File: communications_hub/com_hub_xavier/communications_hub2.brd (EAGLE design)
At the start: 68 x 33 mm, 49 parts, among them CON1 SM04B-GHS-TB, CON2 SM04B-GHS-TB, CON3 SM02B-GHS-TB, CON6 UAVCAN_MICRO, CON7 UAVCAN_MICRO, Q1 DMN5L06K, Q2 DMN5L06K, U1 TCAN1042HVDR, U2 TCAN1042HVDR

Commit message: The board layout is completed.
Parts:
- moved Q2 96.7 mm to (62.2, 8.89)
- moved R19 95.4 mm to (58.4, 27.9), turned to 180 degrees
- moved GPIO_EXP_P17 83.1 mm to (27.9, 30.5)
- moved R13 79.5 mm to (35.6, 29.2)
- moved R21 78.3 mm to (48.3, 8.89)
- moved R22 74.8 mm to (53.3, 8.89)
- moved TP1 63.4 mm to (36.8, 2.54)
- moved TP2 62.7 mm to (33.0, 2.54)
- moved TP3 62.1 mm to (29.2, 2.54)
- moved U$4 57.9 mm to (61.0, 22.9)
- moved R7 55.8 mm to (33.0, 25.4)
- moved SJ1 54.7 mm to (66.0, 14.0), turned to 90 degrees
- moved C2 53.9 mm to (22.9, 25.4), turned to 270 degrees
- moved R5 52.6 mm to (8.89, 30.5)
- moved R14 52.4 mm to (52.1, 29.2)
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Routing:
- net GND: track 0.00 -> 300.0 mm, vias 0 -> 22
- net +3V3: track 0.00 -> 204.5 mm, vias 0 -> 10
- net +5V: track 0.00 -> 125.2 mm, vias 0 -> 3
- net I2C_GP0_SDA: track 0.00 -> 86.9 mm, vias 0 -> 2
- net I2C_GP0_SCL: track 0.00 -> 77.4 mm, vias 0 -> 2
- net CAN0_TX_T: track 0.00 -> 73.2 mm, vias 0 -> 2
- net N$9: track 0.00 -> 56.3 mm
- net N$21: track 0.00 -> 55.6 mm
- net N$14: track 0.00 -> 53.6 mm, vias 0 -> 2
- net N$23: track 0.00 -> 51.9 mm
- net N$22: track 0.00 -> 50.5 mm
- net N$13: track 0.00 -> 47.6 mm
- net CAN0_RX_T: track 0.00 -> 38.3 mm, vias 0 -> 2
- net N$24: track 0.00 -> 34.8 mm
- net N$7: track 0.00 -> 33.8 mm
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- added copper zone on layer 1, net GND

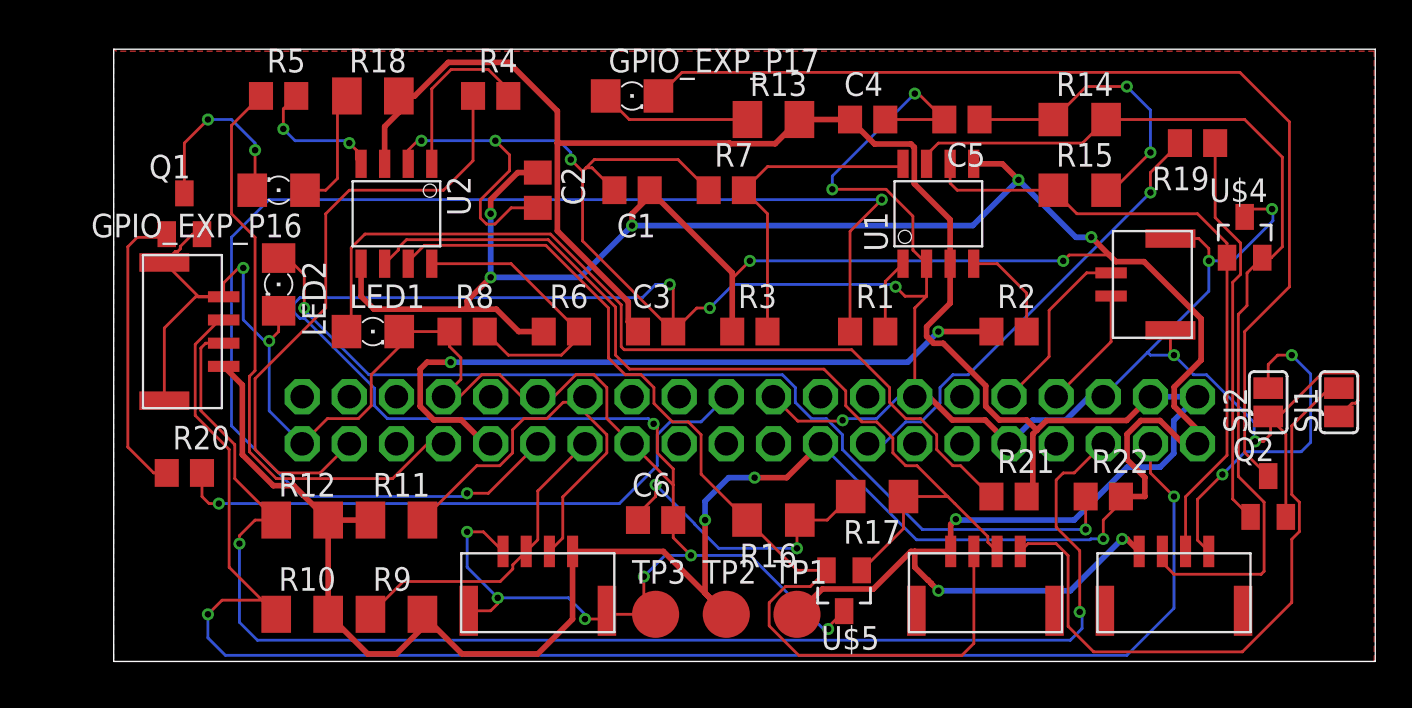
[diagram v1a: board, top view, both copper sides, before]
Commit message: Extra traces are removed, gound plane is added. Default DRC is passed. Info of the board is added as well.
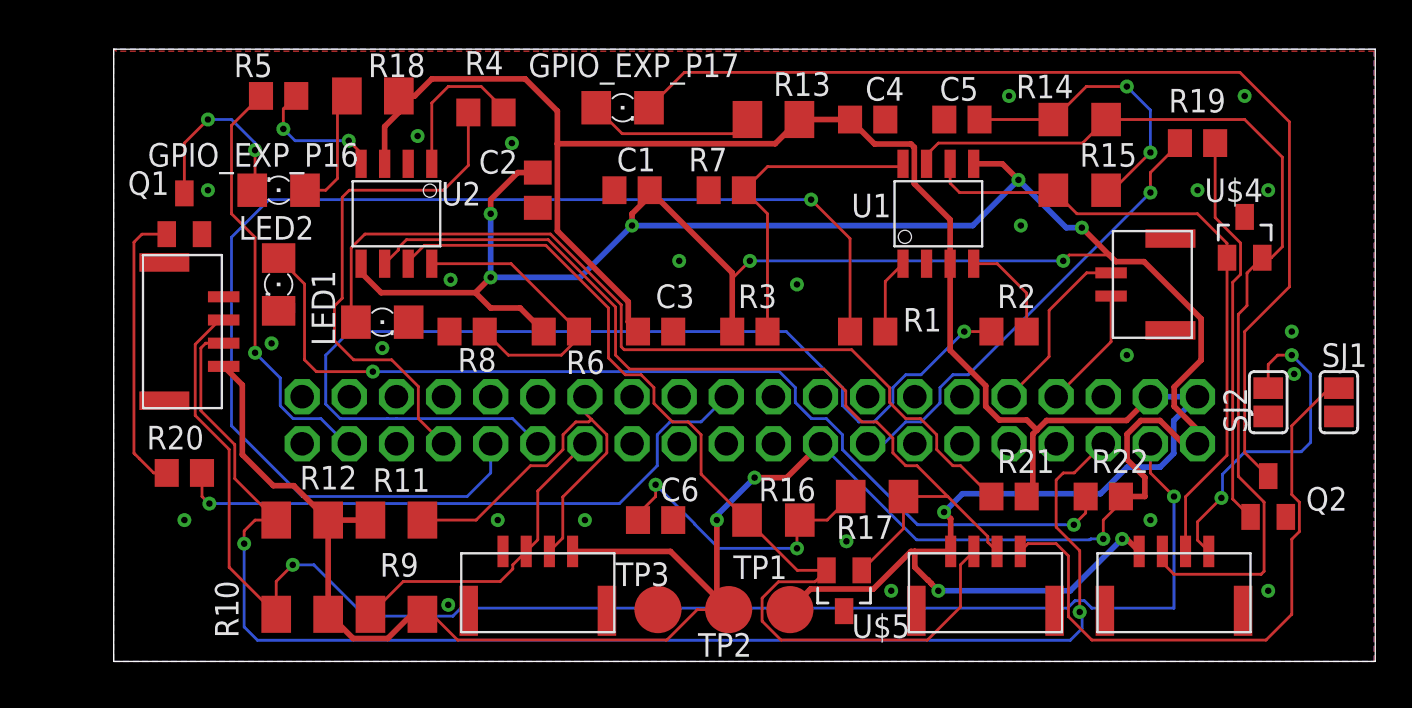
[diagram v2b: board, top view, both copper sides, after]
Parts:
- moved R4 0.92 mm to (20.1, 29.6)
- moved GPIO_EXP_P17 0.81 mm to (27.4, 29.8)
- moved LED1 0.72 mm to (14.5, 18.3)
- moved TP1 0.46 mm to (36.4, 2.79)
- moved TP3 0.28 mm to (29.3, 2.79)
- moved TP2 0.28 mm to (33.1, 2.79)
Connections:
- net CAN0_RX_T: now also JP21.29; no longer JP21.31
- net CAN0_TX_T: now also JP21.31; no longer JP21.29
- net CAN1_RX_T: now also JP21.37; no longer JP21.33
- net CAN1_TX_T: now also JP21.33; no longer JP21.37
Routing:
- net GND: track 300.0 -> 0.46 mm, vias 22 -> 24
- net CAN0_RX_T: track 38.3 -> 56.4 mm, vias 2 -> 1
- net CAN1_RX_T: track 32.3 -> 23.0 mm, vias 0 -> 1
- net I2C_GP0_SDA: track 86.9 -> 80.0 mm
- net CAN1_TX_T: track 33.1 -> 27.5 mm
- net CAN0_TX_T: track 73.2 -> 67.9 mm, vias 2 -> 1
- net N$21: track 55.6 -> 54.1 mm
- net N$28: track 9.39 -> 8.21 mm
- net +5V: track 125.2 -> 124.2 mm
- net N$3: track 8.17 -> 9.04 mm
- net N$9: track 56.3 -> 57.0 mm
- net N$13: track 47.6 -> 47.1 mm
- added copper zone on layer 16, net GND
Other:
- board text added: "Communications Hub Rev. 3.0 Karen Han 2019"

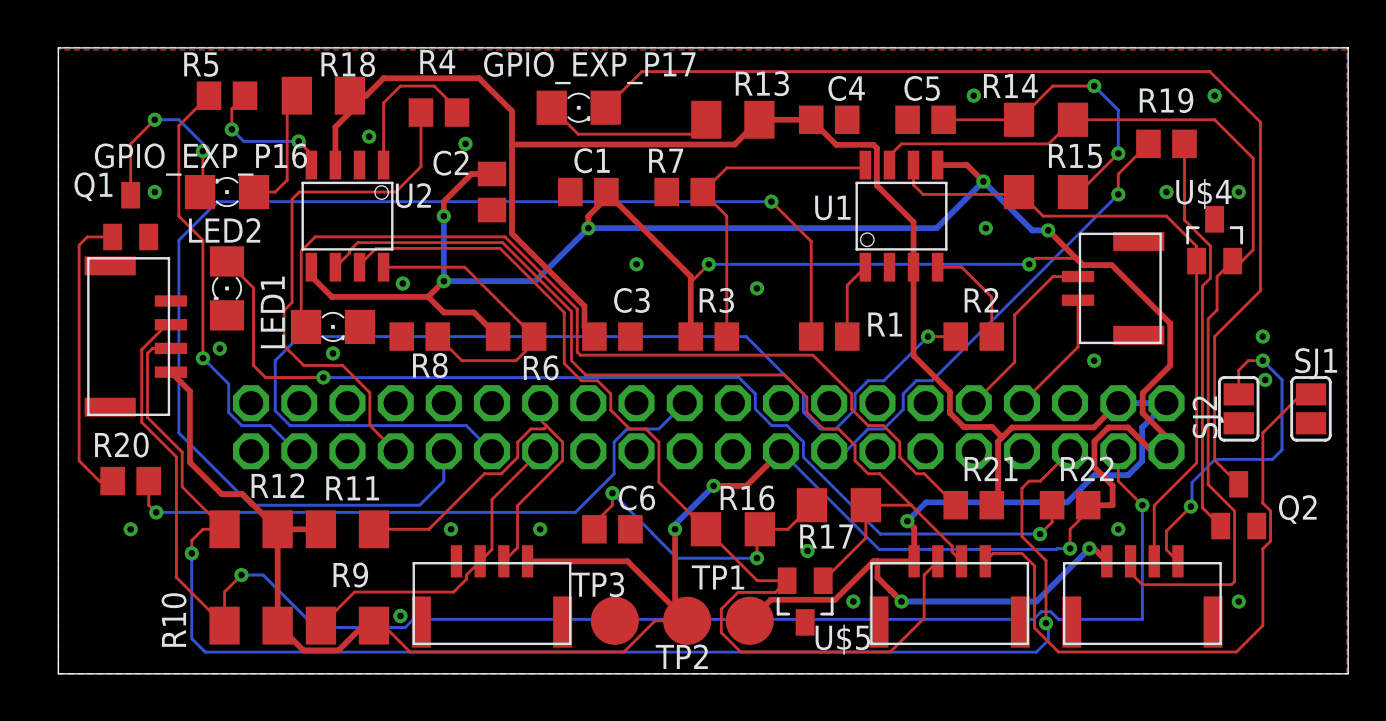
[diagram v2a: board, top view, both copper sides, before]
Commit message: Routed a couple airwires thrown in the DRC, modified some silkscreen. Project still requires BOM.
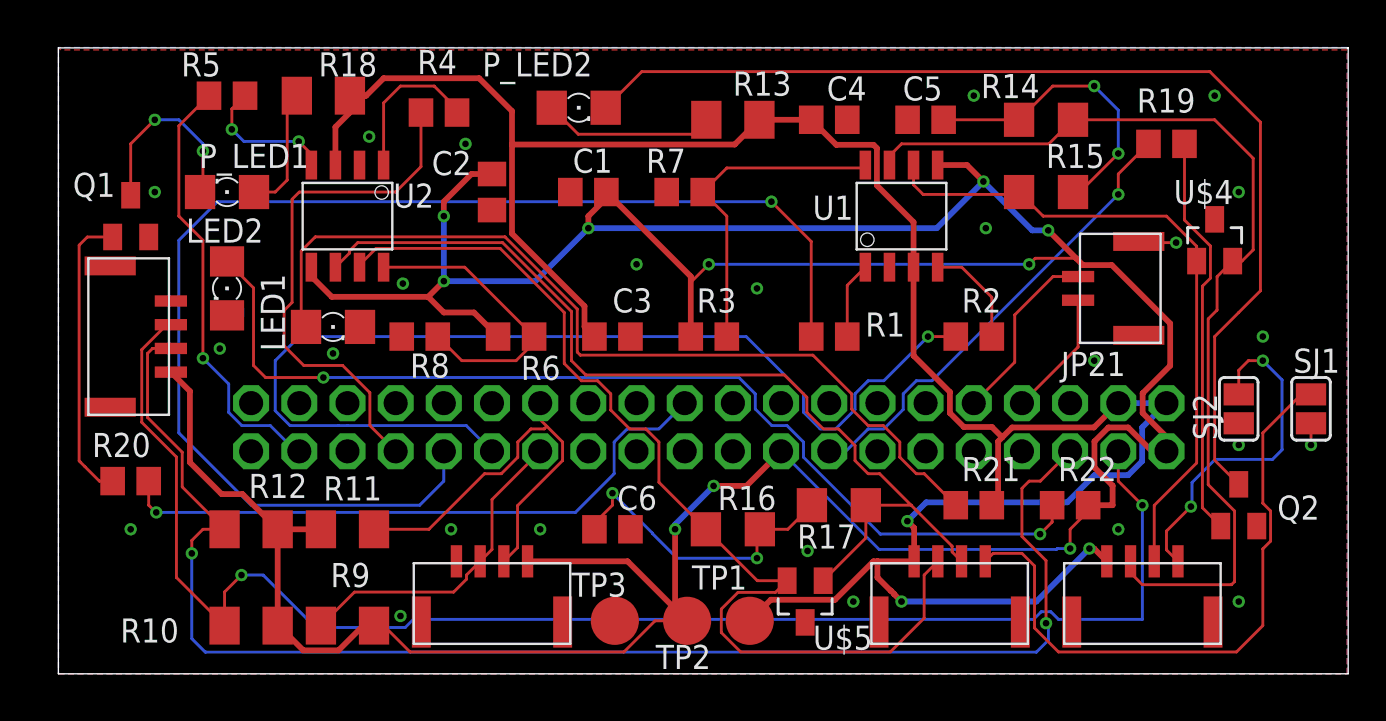
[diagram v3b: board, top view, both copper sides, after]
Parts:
- renumbered GPIO_EXP_P16 to P_LED1, GPIO_EXP_P17 to P_LED2
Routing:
- net GND: track 0.46 -> 3.60 mm, vias 24 -> 25
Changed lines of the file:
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@@
 <?xml version="1.0" encoding="utf-8"?>
 <!DOCTYPE eagle SYSTEM "eagle.dtd">
-<eagle version="9.4.0">
+<eagle version="9.2.2">
 <drawing>
 <settings>
@@
 <setting verticaltext="up"/>
 </settings>
-<grid distance="50" unitdist="mil" unit="mil" style="dots" multiple="1" display="yes" altdistance="5" altunitdist="mil" altunit="mil"/>
+<grid distance="50" unitdist="mil" unit="mil" style="dots" multiple="1" display="no" altdistance="5" altunitdist="mil" altunit="mil"/>
 <layers>
 <layer number="1" name="Top" color="4" fill="1" visible="yes" active="yes"/>
@@
 </class>
 </classes>
-<designrules name="default">
+<designrules name="JLCPCB2Layer">
 <description language="de">&lt;b&gt;EAGLE Design Rules&lt;/b&gt;
 &lt;p&gt;
@@
 necessary adjustments and save your customized
 design rules under a new name.</description>
+<description language="zh">&lt;b&gt;Seeed Studio EAGLE Design Rules&lt;/b&gt;
+</description>
 <param name="layerSetup" value="(1*16)"/>
 <param name="mtCopper" value="0.035mm 0.035mm 0.035mm 0.035mm 0.035mm 0.035mm 0.035mm 0.035mm 0.035mm 0.035mm 0.035mm 0.035mm 0.035mm 0.035mm 0.035mm 0.035mm"/>
@@
 <param name="mdPadVia" value="6mil"/>
 <param name="mdViaVia" value="6mil"/>
-<param name="mdSmdPad" value="6mil"/>
-<param name="mdSmdVia" value="6mil"/>
-<param name="mdSmdSmd" value="6mil"/>
-<param name="mdViaViaSameLayer" value="6mil"/>
+<param name="mdSmdPad" value="0mil"/>
+<param name="mdSmdVia" value="0mil"/>
+<param name="mdSmdSmd" value="0mil"/>
+<param name="mdViaViaSameLayer" value="8mil"/>
 <param name="mnLayersViaInSmd" value="2"/>
-<param name="mdCopperDimension" value="40mil"/>
-<param name="mdDrill" value="6mil"/>
+<param name="mdCopperDimension" value="10mil"/>
+<param name="mdDrill" value="10mil"/>
 <param name="mdSmdStop" value="0mil"/>
 <param name="msWidth" value="6mil"/>
-<param name="msDrill" value="0.35mm"/>
-<param name="msMicroVia" value="9.99mm"/>
+<param name="msDrill" value="10mil"/>
+<param name="msMicroVia" value="10mil"/>
 <param name="msBlindViaRatio" value="0.5"/>
 <param name="rvPadTop" value="0.25"/>
@@
 <param name="rvMicroViaOuter" value="0.25"/>
 <param name="rvMicroViaInner" value="0.25"/>
-<param name="rlMinPadTop" value="10mil"/>
+<param name="rlMinPadTop" value="6mil"/>
 <param name="rlMaxPadTop" value="20mil"/>
-<param name="rlMinPadInner" value="10mil"/>
+<param name="rlMinPadInner" value="6mil"/>
 <param name="rlMaxPadInner" value="20mil"/>
-<param name="rlMinPadBottom" value="10mil"/>
+<param name="rlMinPadBottom" value="6mil"/>
 <param name="rlMaxPadBottom" value="20mil"/>
-<param name="rlMinViaOuter" value="8mil"/>
+<param name="rlMinViaOuter" value="6mil"/>
 <param name="rlMaxViaOuter" value="20mil"/>
-<param name="rlMinViaInner" value="8mil"/>
+<param name="rlMinViaInner" value="6mil"/>
 <param name="rlMaxViaInner" value="20mil"/>
 <param name="rlMinMicroViaOuter" value="4mil"/>
@@
 <param name="psTop" value="-1"/>
 <param name="psBottom" value="-1"/>
-<param name="psFirst" value="-1"/>
+<param name="psFirst" value="0"/>
 <param name="psElongationLong" value="100"/>
 <param name="psElongationOffset" value="100"/>
 <param name="mvStopFrame" value="1"/>
 <param name="mvCreamFrame" value="0"/>
-<param name="mlMinStopFrame" value="4mil"/>
-<param name="mlMaxStopFrame" value="4mil"/>
+<param name="mlMinStopFrame" value="2mil"/>
+<param name="mlMaxStopFrame" value="2mil"/>
 <param name="mlMinCreamFrame" value="0mil"/>
 <param name="mlMaxCreamFrame" value="0mil"/>
-<param name="mlViaStopLimit" value="0mil"/>
+<param name="mlViaStopLimit" value="100mil"/>
 <param name="srRoundness" value="0"/>
 <param name="srMinRoundness" value="0mil"/>
@@
 <param name="checkAngle" value="0"/>
 <param name="checkFont" value="1"/>
-<param name="checkRestrict" value="1"/>
+<param name="checkRestrict" value="0"/>
 <param name="checkStop" value="0"/>
 <param name="checkValues" value="0"/>
@@
 <element name="CON2" library="ARVP" package="SM04B-GHS-TB" value="SM04B-GHS-TB" x="5.08" y="17.78" smashed="yes" rot="R270"/>
 <element name="CON3" library="ARVP" package="SM02B-GHS-TB" value="SM02B-GHS-TB" x="54.61" y="20.32" smashed="yes" rot="R90"/>
-<element name="GPIO_EXP_P16" library="eagle-ltspice" library_urn="urn:adsk.eagle:library:217" package="LED_1206" package3d_urn="urn:adsk.eagle:package:13319/1" value="XZDG55W-3" x="8.89" y="25.4" smashed="yes" rot="R180">
+<element name="P_LED1" library="eagle-ltspice" library_urn="urn:adsk.eagle:library:217" package="LED_1206" package3d_urn="urn:adsk.eagle:package:13319/1" value="XZDG55W-3" x="8.89" y="25.4" smashed="yes" rot="R180">
 <attribute name="NAME" x="13.208" y="27.94" size="1.27" layer="25" rot="R180"/>
 <attribute name="SPICEMODEL" value="NONE" x="-33.02" y="54.61" size="1.778" layer="27" rot="R180" display="off"/>
@@
 <attribute name="SPICETYPE" value="diode" x="-33.02" y="54.61" size="1.778" layer="27" rot="R180" display="off"/>
 </element>
-<element name="GPIO_EXP_P17" library="eagle-ltspice" library_urn="urn:adsk.eagle:library:217" package="LED_1206" package3d_urn="urn:adsk.eagle:package:13319/1" value="XZM2ACR55W-3" x="27.432" y="29.845" smashed="yes">
+<element name="P_LED2" library="eagle-ltspice" library_urn="urn:adsk.eagle:library:217" package="LED_1206" package3d_urn="urn:adsk.eagle:package:13319/1" value="XZM2ACR55W-3" x="27.432" y="29.845" smashed="yes">
 <attribute name="NAME" x="22.352" y="31.496" size="1.27" layer="25"/>
 <attribute name="SPICEMODEL" value="NONE" x="54.102" y="0.635" size="1.778" layer="27" display="off"/>
@@
 </element>
 <element name="JP21" library="commhub" package="2X20" value="" x="34.29" y="13" smashed="yes" rot="MR0">
-<attribute name="NAME" x="53.721" y="16.972" size="1.27" layer="26" ratio="10" rot="MR180"/>
+<attribute name="NAME" x="56.261" y="16.972" size="1.27" layer="25" ratio="10" rot="R180"/>
 <attribute name="VALUE" x="59.69" y="8.555" size="1.27" layer="28" rot="MR0"/>
 </element>
@@
 </element>
 <element name="R10" library="resistor" library_urn="urn:adsk.eagle:library:348" package="M1206" package3d_urn="urn:adsk.eagle:package:23566/1" value="10K" x="10.16" y="2.54" smashed="yes">
-<attribute name="NAME" x="6.731" y="1.27" size="1.27" layer="25" rot="R90"/>
+<attribute name="NAME" x="6.35" y="2.921" size="1.27" layer="25" rot="R180"/>
 </element>
 <element name="R11" library="resistor" library_urn="urn:adsk.eagle:library:348" package="M1206" package3d_urn="urn:adsk.eagle:package:23566/1" value="10K" x="15.24" y="7.62" smashed="yes">
@@
 <via x="30.48" y="21.59" extent="1-16" drill="0.35"/>
 <via x="48.895" y="23.495" extent="1-16" drill="0.35"/>
-<via x="58.42" y="25.4" extent="1-16" drill="0.35"/>
 <via x="60.96" y="30.48" extent="1-16" drill="0.35"/>
 <via x="48.26" y="30.48" extent="1-16" drill="0.35"/>
@@
 <via x="8.509" y="17.145" extent="1-16" drill="0.35"/>
 <via x="14.478" y="16.891" extent="1-16" drill="0.35"/>
-<via x="63.627" y="15.494" extent="1-16" drill="0.35"/>
+<via x="62.23" y="12.065" extent="1-16" drill="0.35"/>
+<wire x1="66.04" y1="13.208" x2="66.04" y2="12.065" width="0.1524" layer="1"/>
+<via x="66.04" y="12.065" extent="1-16" drill="0.35"/>
+<wire x1="58.928" y1="22.733" x2="57.022" y2="22.733" width="0.1524" layer="1"/>
+<wire x1="56.96" y1="22.795" x2="57.022" y2="22.733" width="0.1524" layer="1"/>
+<via x="58.928" y="22.733" extent="1-16" drill="0.35"/>
 </signal>
 <signal name="+3V3">
@@
 </signal>
 <signal name="N$3">
-<contactref element="GPIO_EXP_P17" pad="A"/>
+<contactref element="P_LED2" pad="A"/>
 <contactref element="R13" pad="1"/>
 <wire x1="26.01" y1="29.845" x2="27.407" y2="28.448" width="0.1524" layer="1"/>
@@
 </signal>
 <signal name="N$4">
-<contactref element="GPIO_EXP_P16" pad="A"/>
+<contactref element="P_LED1" pad="A"/>
 <contactref element="R18" pad="1"/>
 <wire x1="12.57" y1="30.48" x2="12.062" y2="29.972" width="0.1524" layer="1"/>
@@
 </signal>
 <signal name="N$9">
-<contactref element="GPIO_EXP_P17" pad="C"/>
+<contactref element="P_LED2" pad="C"/>
 <contactref element="Q2" pad="3"/>
 <wire x1="28.854" y1="29.845" x2="30.759" y2="31.75" width="0.1524" layer="1"/>
@@
 <wire x1="60.706" y1="31.75" x2="63.373" y2="29.083" width="0.1524" layer="1"/>
 <wire x1="63.373" y1="29.083" x2="63.373" y2="20.193" width="0.1524" layer="1"/>
-<wire x1="63.373" y1="20.193" x2="60.96" y2="17.78" width="0.1524" layer="1"/>
+<wire x1="63.373" y1="20.193" x2="62.23" y2="19.05" width="0.1524" layer="1"/>
+<wire x1="62.23" y1="19.05" x2="60.96" y2="17.78" width="0.1524" layer="1"/>
 <wire x1="60.96" y1="17.78" x2="60.96" y2="11.26" width="0.1524" layer="1"/>
 <wire x1="60.96" y1="11.26" x2="62.23" y2="9.99" width="0.1524" layer="1"/>
 </signal>
 <signal name="N$10">
-<contactref element="GPIO_EXP_P16" pad="C"/>
+<contactref element="P_LED1" pad="C"/>
 <contactref element="Q1" pad="3"/>
 <wire x1="3.81" y1="25.23" x2="3.81" y2="27.94" width="0.1524" layer="1"/>
